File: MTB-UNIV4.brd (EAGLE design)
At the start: 100 x 80 mm, 95 parts, among them IC1 MEGA128-A, IC2 SN75176BP, IC3 MC7805CDTG, IC4 ULN2803A, IC5 ULN2803A, X1 CON-04-5.0CON-5MM, X2 CON-04-5.0CON-5MM

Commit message: Přidány konektory a patice dle požadavků a přidána přepěťová ochrana jako u výstupů
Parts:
- removed JP10, JP11, JP12, JP13, JP14, JP8, JP9: 22-05-7038-03, con-molex:7395-03
- added C18, C19, C20, C21: 100nF, rcl:C1206
- added D10, D11, D12, D13, D14, D15, D16, D17, D18, D19, D20, D21, D6, D7, D8, D9: SCHOTTKY_LM5819, ElectroKrt:DIOMELF3516
- added D22, D5: (no value), diode:SOT23
- added F18, F19, F20, F21, F22, F23, F24, F25, F26, F27, F28, F29, F30, F31, F32, F33: (no value), adafruit:1812
- added R23, R24: 2k2, rcl:R1206
- added TH4, TH5: MCR100, ElectroKrt:TO92
- added X4, X5, X6: 1751316, con-phoenix-350:1751316
- JP2: device adafruit:1X09-BIG -> con-phoenix-254:2POL254
- JP3, JP4, JP5: value (none) -> 22-05-7098-09; device adafruit:1X09-BIG -> con-molex:7395-09
- JP6: value (none) -> 22-05-7098-09; device SparkFun-Connectors:2X8 -> con-molex:7395-09
- JP7: value 22-05-7038-03 -> (none); device con-molex:7395-03 -> SparkFun-Connectors:2X8
- X3: value (none) -> 1751316; device con-phoenix-254:2POL254 -> con-phoenix-350:1751316
- moved X3 672.9 mm to (-182.9, -848.4)
- moved JP2 556.7 mm to (-67.3, -185.4)
- moved JP6 392.5 mm to (-179.1, -820.4)
- moved JP7 309.1 mm to (-74.9, -442.0)
- moved JP5 174.0 mm to (-176.5, -802.6)
- moved JP4 173.9 mm to (-174.0, -784.9)
- moved JP3 169.9 mm to (-171.4, -767.1)
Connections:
- new net N$62: D6.2, F18.1, R3.2
- new net N$63: D7.2, F19.1, R4.2
- new net N$64: D8.2, F20.1, R5.2
- new net N$65: D9.2, F21.1, R6.2
- new net N$66: D10.2, F22.1, R7.2
- new net N$67: D11.2, F23.1, R8.2
- new net N$68: D12.2, F24.1, R9.2
- new net N$69: D13.2, F25.1, R10.2
- new net N$70: C18.1, D10.1, D11.1, D12.1, D13.1, D5.3, D6.1, D7.1, D8.1, D9.1, TH4.3
- new net N$71: C19.2, D5.1, R23.2, TH4.2
- new net N$72: D14.2, F26.1, R11.2
- new net N$73: D15.2, F27.1, R12.2
- new net N$74: D16.2, F28.1, R13.2
- new net N$75: D17.2, F29.1, R14.2
- new net N$76: D18.2, F30.1, R15.2
- new net N$77: D19.2, F31.1, R16.2
- new net N$78: D20.2, F32.1, R17.2
- new net N$79: D21.2, F33.1, R18.2
- new net N$80: C20.1, D14.1, D15.1, D16.1, D17.1, D18.1, D19.1, D20.1, D21.1, D22.3, TH5.3
- new net N$81: C21.1, D22.1, R24.2, TH5.2
- net ADDR-1: now also JP7.1; no longer JP6.1
- net ADDR-2: now also JP7.3; no longer JP6.3
- net ADDR-3: now also JP7.5; no longer JP6.5
- net ADDR-4: now also JP7.7; no longer JP6.7
- net ADDR-5: now also JP7.9; no longer JP6.9
- net ADDR-6: now also JP7.11; no longer JP6.11
- net ADDR-7: now also JP7.13; no longer JP6.13
- net ADDR-8: now also JP7.15; no longer JP6.15
- net D-IN(A)1: now also RN1.2; no longer RN1.9
- net D-IN(A)2: now also RN1.3; no longer RN1.8
- net D-IN(A)3: now also RN1.4; no longer RN1.7
- net D-IN(A)4: now also RN1.5; no longer RN1.6
- net D-IN(A)5: now also RN1.6; no longer RN1.5
- net D-IN(A)6: now also RN1.7; no longer RN1.4
- net D-IN(A)7: now also RN1.8; no longer RN1.3
- net D-IN(A)8: now also RN1.9; no longer RN1.2
- net D-IN(B)1: now also RN2.2; no longer RN2.9
- net D-IN(B)2: now also RN2.3; no longer RN2.8
- net D-IN(B)3: now also RN2.4; no longer RN2.7
- net D-IN(B)4: now also RN2.5; no longer RN2.6
- net D-IN(B)5: now also RN2.6; no longer RN2.5
- net D-IN(B)6: now also RN2.7; no longer RN2.4
- net D-IN(B)7: now also RN2.8; no longer RN2.3
- net D-IN(B)8: now also RN2.9; no longer RN2.2
- net GND: now also C18.2, C19.1, C20.2, C21.2, JP2.1, JP6.9, JP7.10, JP7.12, JP7.14, JP7.16, JP7.2, JP7.4, JP7.6, JP7.8, R23.1, R24.1, TH4.1, TH5.1, X3.9, X4.9, X5.9, X6.9; no longer JP10.3, JP11.3, JP12.3, JP13.3, JP14.3, JP2.9, JP6.10, JP6.12, JP6.14, JP6.16, JP6.2, JP6.4, JP6.6, JP6.8, JP7.3, JP8.3, JP9.3, X3.1
- net N$10: now also JP3.8, X3.8; no longer JP14.2, JP2.8
- net N$12: now also JP4.1, X4.1; no longer JP3.1
- net N$15: now also JP4.2, X4.2; no longer JP3.2
- net N$16: now also JP4.3, X4.3; no longer JP3.3
- net N$17: now also JP4.4, X4.4; no longer JP3.4
- net N$18: now also JP4.5, X4.5; no longer JP3.5
- net N$19: now also JP4.6, X4.6; no longer JP3.6
- net N$2: now also JP3.1, X3.1; no longer JP2.1, JP7.2
- net N$20: now also JP4.7, X4.7; no longer JP3.7
- net N$21: now also F26.2, JP6.1, X6.1; no longer JP5.1, R11.2
- net N$22: now also F27.2, JP6.2, X6.2; no longer JP5.2, R12.2
- net N$23: now also F28.2, JP6.3, X6.3; no longer JP5.3, R13.2
- net N$24: now also F29.2, JP6.4, X6.4; no longer JP5.4, R14.2
- net N$25: now also F30.2, JP6.5, X6.5; no longer JP5.5, R15.2
- net N$26: now also F31.2, JP6.6, X6.6; no longer JP5.6, R16.2
- net N$27: now also F32.2, JP6.7, X6.7; no longer JP5.7, R17.2
- net N$28: now also F33.2, JP6.8, X6.8; no longer JP5.8, R18.2
- net N$29: now also F18.2, JP5.1, X5.1; no longer JP4.1, R3.2
- net N$30: now also F19.2, JP5.2, X5.2; no longer JP4.2, R4.2
- net N$31: now also F20.2, JP5.3, X5.3; no longer JP4.3, R5.2
- net N$32: now also F21.2, JP5.4, X5.4; no longer JP4.4, R6.2
- net N$33: now also F22.2, JP5.5, X5.5; no longer JP4.5, R7.2
- net N$34: now also F23.2, JP5.6, X5.6; no longer JP4.6, R8.2
- net N$35: now also F24.2, JP5.7, X5.7; no longer JP4.7, R9.2
- net N$36: now also F25.2, JP5.8, X5.8; no longer JP4.8, R10.2
- net N$4: now also JP3.2, X3.2; no longer JP2.2, JP8.2
- net N$47: now also JP4.8, X4.8; no longer JP3.8
- net N$5: now also JP3.3, X3.3; no longer JP2.3, JP9.2
- net N$6: now also JP3.4, X3.4; no longer JP10.2, JP2.4
- net N$7: now also JP3.5, X3.5; no longer JP11.2, JP2.5
- net N$8: now also JP3.6, X3.6; no longer JP12.2, JP2.6
- net N$9: now also JP3.7, X3.7; no longer JP13.2, JP2.7
- net RST: now also JP2.2; no longer X3.2

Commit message: Rozmístěnjy součástky na desku, první kroky routingu. Opraveny drobné nedostatky
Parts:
- added C22: 100nF, rcl:C1206
- added H1, H2, H3, H4: MOUNT-PAD-ROUND3.2, holes:3,2-PAD
- moved D13 1106.5 mm to (4.09, 20.5), turned to 270 degrees
- moved D12 1098.8 mm to (7.94, 20.5), turned to 270 degrees
- moved D11 1091.1 mm to (11.8, 20.5), turned to 270 degrees
- moved D10 1083.4 mm to (15.6, 20.5), turned to 270 degrees
- moved D9 1075.7 mm to (19.5, 20.5), turned to 270 degrees
- moved D8 1068.0 mm to (23.3, 20.5), turned to 270 degrees
- moved D7 1060.3 mm to (27.2, 20.5), turned to 270 degrees
- moved D6 1052.6 mm to (31.0, 20.5), turned to 270 degrees
- moved F33 1039.9 mm to (36.5, 13.8), turned to 270 degrees
- moved F32 1034.6 mm to (40.4, 13.8), turned to 270 degrees
- moved F31 1029.3 mm to (44.2, 13.8), turned to 270 degrees
- moved F30 1024.0 mm to (48.1, 13.8), turned to 270 degrees
- moved F29 1018.8 mm to (51.9, 13.8), turned to 270 degrees
- moved F28 1013.6 mm to (55.8, 13.8), turned to 270 degrees
- moved TH4 1010.8 mm to (14.0, 38.4), turned to 90 degrees
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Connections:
- removed net V+: F1.P$1
- net +12V: now also F1.P$1
- net +5V: now also C22.1
- net ADDR-1: now also IC1.15; no longer IC1.5
- net ADDR-2: now also IC1.14; no longer IC1.6
- net ADDR-3: now also IC1.10; no longer IC1.7
- net ADDR-4: now also IC1.9; no longer IC1.8
- net ADDR-5: now also IC1.8; no longer IC1.9
- net ADDR-6: now also IC1.7; no longer IC1.10
- net ADDR-7: now also IC1.6; no longer IC1.14
- net ADDR-8: now also IC1.5; no longer IC1.15
- net D-IN(B)1: now also IC1.61; no longer IC1.35
- net D-IN(B)2: now also IC1.60; no longer IC1.36
- net D-IN(B)3: now also IC1.59; no longer IC1.37
- net D-IN(B)4: now also IC1.58; no longer IC1.38
- net D-IN(B)5: now also IC1.57; no longer IC1.39
- net D-IN(B)6: now also IC1.56; no longer IC1.40
- net D-IN(B)7: now also IC1.55; no longer IC1.41
- net D-IN(B)8: now also IC1.54; no longer IC1.42
- net D-OUT(A)1: now also IC1.42; no longer IC1.25
- net D-OUT(A)2: now also IC1.41; no longer IC1.26
- net D-OUT(A)3: now also IC1.40; no longer IC1.27
- net D-OUT(A)4: now also IC1.39; no longer IC1.28
- net D-OUT(A)5: now also IC1.38; no longer IC1.29
- net D-OUT(A)6: now also IC1.37; no longer IC1.30
- net D-OUT(A)7: now also IC1.36; no longer IC1.31
- net D-OUT(A)8: now also IC1.35; no longer IC1.32
- net D-OUT(B)1: now also IC1.32; no longer IC1.61
- net D-OUT(B)2: now also IC1.31; no longer IC1.60
- net D-OUT(B)3: now also IC1.30; no longer IC1.59
- net D-OUT(B)4: now also IC1.29; no longer IC1.58
- net D-OUT(B)5: now also IC1.28; no longer IC1.57
- net D-OUT(B)6: now also IC1.27; no longer IC1.56
- net D-OUT(B)7: now also IC1.26; no longer IC1.55
- net D-OUT(B)8: now also IC1.25; no longer IC1.54
- net GND: now also C22.2, H1.B3,2, H2.B3,2, H3.B3,2, H4.B3,2
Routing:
- net +5V: track 0.00 -> 112.7 mm, vias 0 -> 1
- net N$70: track 0.00 -> 90.6 mm
- net N$80: track 0.00 -> 89.4 mm
- net RS-A: track 0.00 -> 39.1 mm
- net RS-B: track 0.00 -> 37.0 mm
- net RST: track 0.00 -> 33.8 mm
- net +12V: track 0.00 -> 32.6 mm
- net N$13: track 0.00 -> 32.5 mm
- net N$11: track 0.00 -> 22.6 mm
- net N$37: track 0.00 -> 21.9 mm
- net MISO: track 0.00 -> 18.0 mm
- net N$36: track 0.00 -> 17.4 mm
- net N$28: track 0.00 -> 17.3 mm
- net N$35: track 0.00 -> 16.6 mm
- net N$27: track 0.00 -> 16.6 mm
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
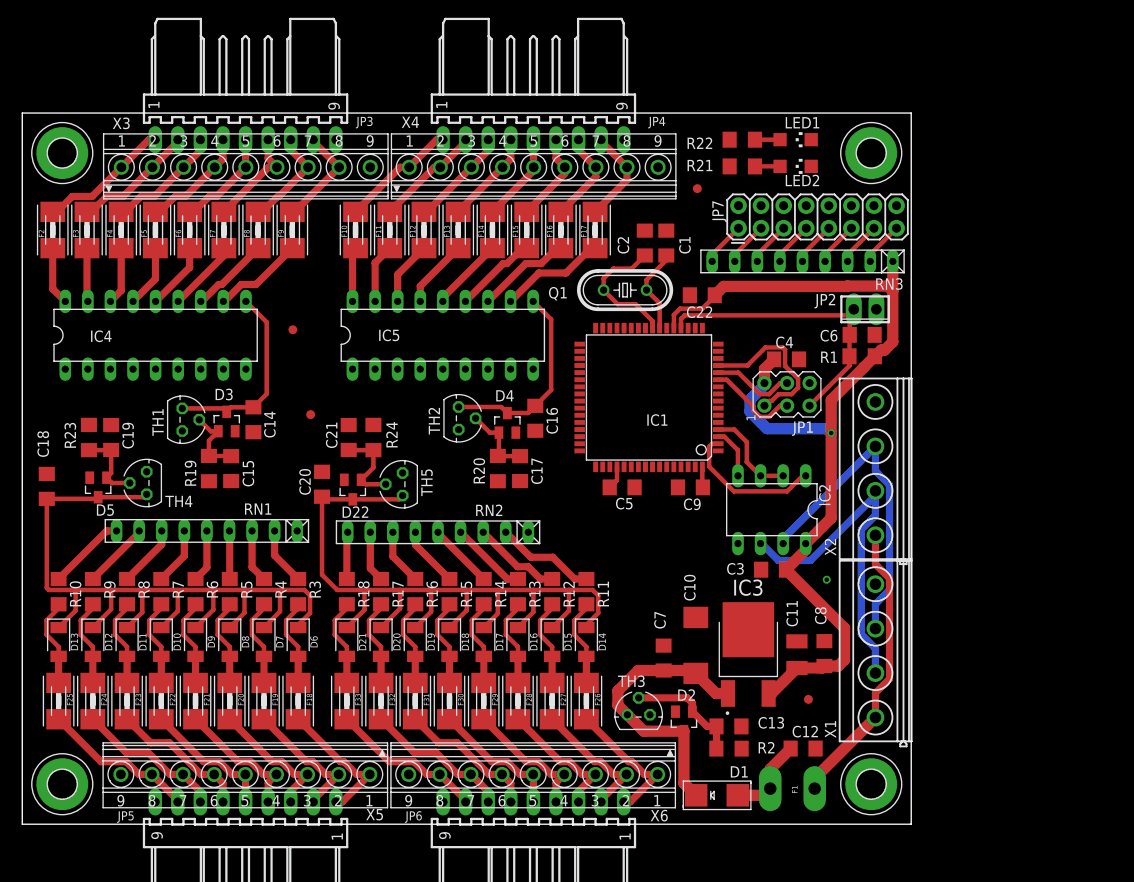
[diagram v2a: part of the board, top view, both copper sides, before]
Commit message: Toto je pokus o naskládání všeho na desku rozměru 106x67mm. Opravdu tam není kam to dát. Nejde o součástky, ale jde o počet spojů. posuvné registry na starých deskách toto vyřešily, ale zde je procesor s 48 piny a přestože je pouze 41 z nich zapojeno, tak 41x0,4mm+40x0,3mm je přes 3 cm a to je opravdu hodně spojů. Nepočítám do toho větvení apod. Menší součástky také nepomohou, protože tam prostě není dost místa.
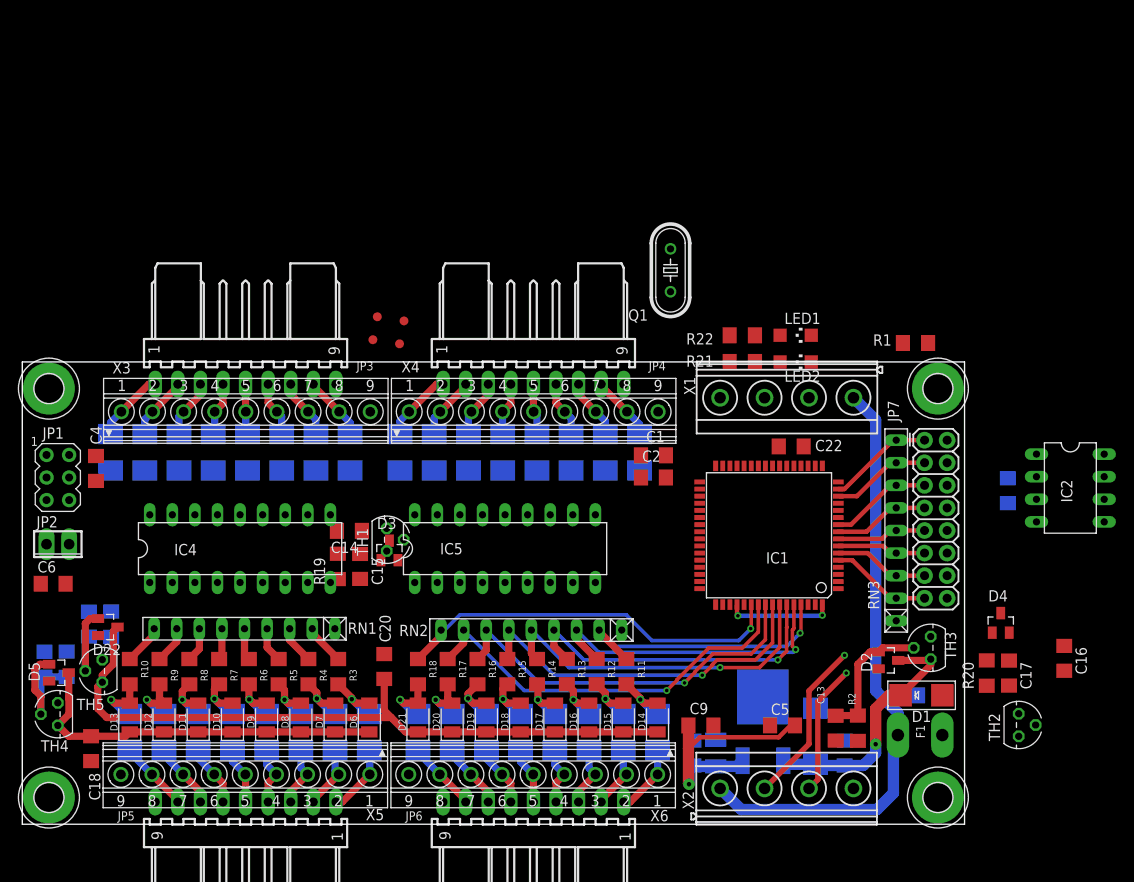
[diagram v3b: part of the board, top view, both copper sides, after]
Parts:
- moved C6 95.2 mm to (3.48, 27.1)
- moved JP2 94.6 mm to (4.00, 31.5)
- moved JP1 82.6 mm to (4.00, 39.0), turned to 0 degrees
- moved C4 78.7 mm to (8.29, 40.0), turned to 270 degrees
- moved TH2 71.8 mm to (112.1, 11.2)
- moved C16 65.3 mm to (117.2, 18.7)
- moved U$3 61.0 mm to (42.4, 54.0)
- moved D4 59.9 mm to (110.1, 22.6)
- moved C17 59.6 mm to (111.0, 17.0)
- moved R20 59.6 mm to (108.5, 17.0)
- moved U$4 40.3 mm to (39.4, 54.5)
- moved TH5 39.8 mm to (9.00, 17.2)
- moved X2 37.4 mm to (86.0, 4.00), turned to 0 degrees
- moved R24 36.2 mm to (10.0, 22.5), flipped to the bottom
- moved C21 36.0 mm to (7.50, 22.5), flipped to the bottom
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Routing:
- net +5V: track 112.7 -> 39.9 mm, vias 1 -> 3
- net N$70: track 90.6 -> 42.2 mm
- net D-IN(B)7: track 5.76 -> 45.8 mm, vias 0 -> 1
- net D-IN(B)8: track 5.30 -> 44.3 mm, vias 0 -> 1
- net D-IN(B)6: track 6.30 -> 43.5 mm, vias 0 -> 1
- net +12V: track 32.6 -> 68.0 mm
- net D-IN(B)5: track 6.84 -> 41.0 mm, vias 0 -> 1
- net RST: track 33.8 -> 0.00 mm
- net D-IN(B)4: track 7.39 -> 38.9 mm, vias 0 -> 1
- net D-IN(B)3: track 8.63 -> 37.1 mm, vias 0 -> 1
- net D-IN(B)2: track 9.94 -> 35.3 mm, vias 0 -> 1
- net N$11: track 22.6 -> 0.00 mm
- net RS-B: track 37.0 -> 14.7 mm, vias 0 -> 1
- net N$37: track 21.9 -> 0.00 mm
- net D-IN(B)1: track 11.2 -> 31.8 mm, vias 0 -> 1
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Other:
- board size 100 x 80 mm -> 106 x 52 mm

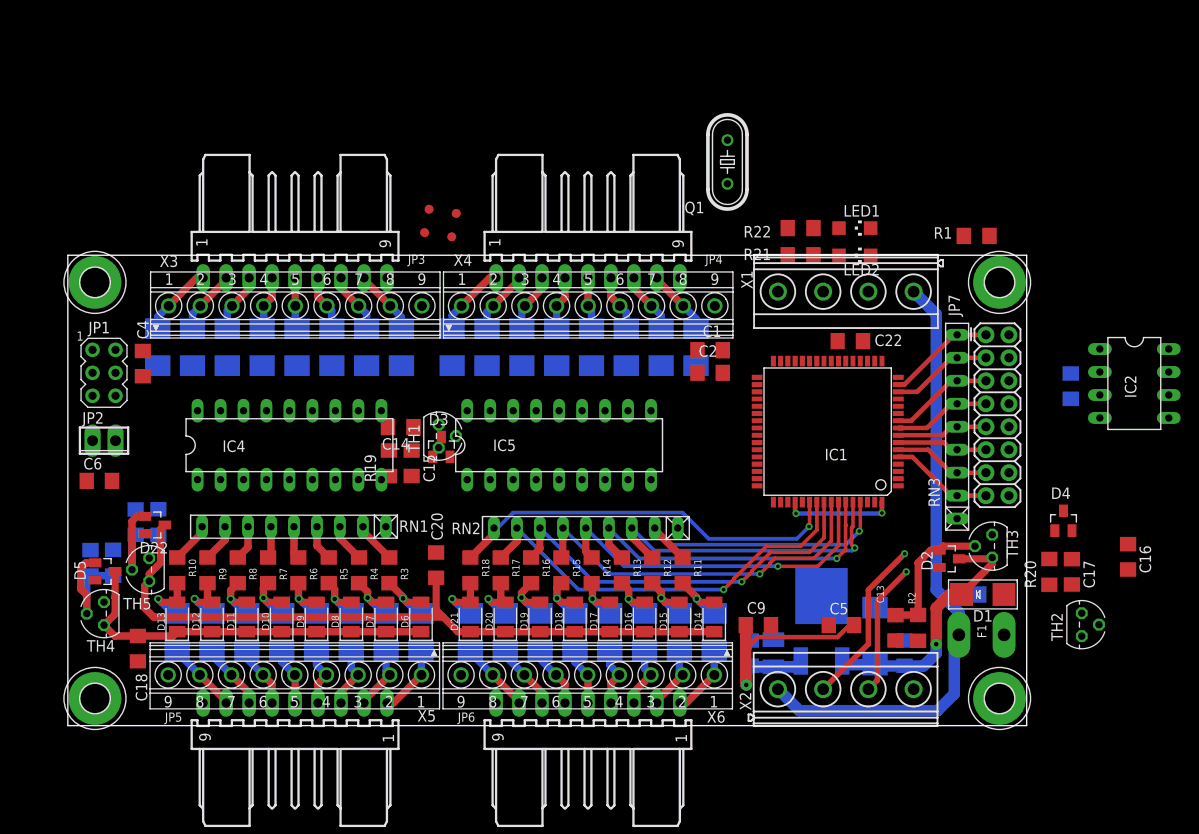
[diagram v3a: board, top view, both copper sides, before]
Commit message: První hotový prototyp MTB nástupce MTB uni s rozměry 106x67mm a roztečí montážních otvorů 100x55mm.
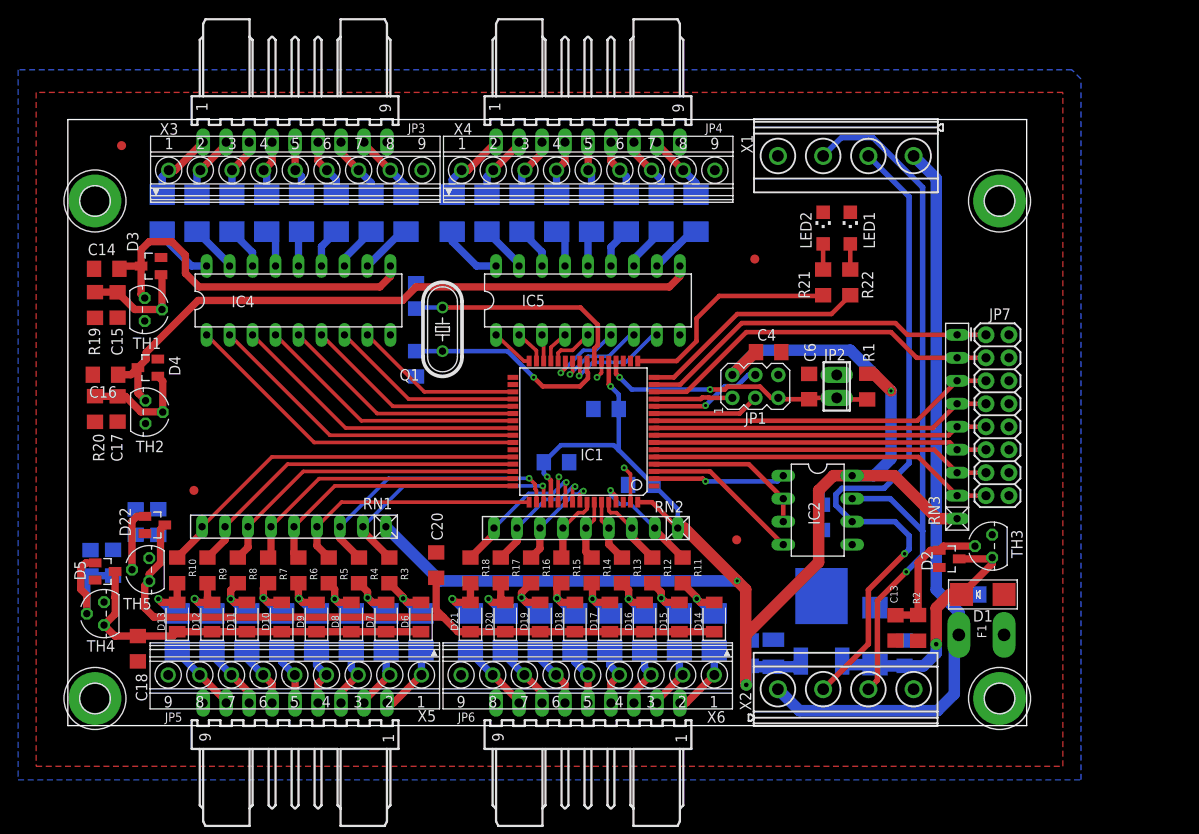
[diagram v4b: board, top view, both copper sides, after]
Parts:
- moved C16 114.8 mm to (4.16, 38.8), turned to 180 degrees
- moved C17 107.0 mm to (5.50, 35.0)
- moved R20 107.0 mm to (3.00, 35.0)
- moved TH2 106.1 mm to (8.59, 34.7)
- moved D4 102.6 mm to (8.85, 39.6), turned to 90 degrees
- moved JP2 81.2 mm to (85.0, 37.5), turned to 270 degrees
- moved C6 79.2 mm to (82.0, 37.5), turned to 90 degrees
- moved JP1 72.0 mm to (76.0, 37.5), turned to 90 degrees
- moved C4 69.2 mm to (77.5, 41.3), turned to 0 degrees
- moved U$3 46.0 mm to (73.9, 20.5)
- moved U$4 38.2 mm to (13.9, 26.0)
- moved D3 37.8 mm to (9.20, 50.8), turned to 90 degrees
- moved U$1 37.8 mm to (5.94, 64.1)
- moved IC2 37.7 mm to (82.9, 23.8)
- moved C14 36.9 mm to (4.30, 50.5)
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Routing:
- net +5V: track 39.9 -> 194.9 mm, vias 3 -> 5
- net N$11: track 0.00 -> 72.2 mm
- net RS-B: track 14.7 -> 81.4 mm
- net RS-A: track 18.7 -> 77.0 mm
- net N$37: track 0.00 -> 40.8 mm
- net D-OUT(A)1: track 0.00 -> 38.8 mm
- net D-IN(A)8: track 4.55 -> 42.1 mm
- net D-OUT(A)2: track 0.00 -> 35.9 mm
- net D-IN(A)7: track 4.21 -> 38.9 mm
- net D-IN(B)5: track 41.0 -> 7.63 mm, vias 1 -> 0
- net D-OUT(A)3: track 0.00 -> 33.0 mm
- net D-IN(B)4: track 38.9 -> 6.77 mm, vias 1 -> 0
- net D-IN(B)6: track 43.5 -> 11.6 mm
- net D-IN(A)6: track 3.88 -> 35.7 mm
- net D-IN(B)7: track 45.8 -> 14.2 mm
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- added copper zone on layer 1, net GND
- added copper zone on layer 16, net GND
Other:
- board size 106 x 52 mm -> 106 x 67 mm
